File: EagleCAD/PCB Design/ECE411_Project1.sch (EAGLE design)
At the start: 38 parts, among them J1 0473460001_USBMICRO, U1 ATS160SM-1, U2 MIC29310-5.0WU, U3 NCP5501DT50RKG, U4 DCJACK_2.1MM_PTH

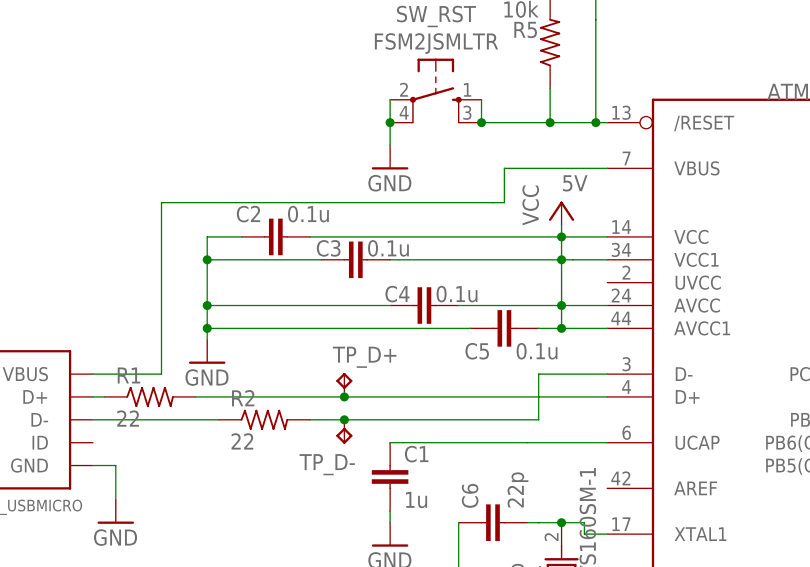
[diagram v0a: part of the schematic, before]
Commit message: In-progress updates: Connected UVCC to power and added a capacitor for it
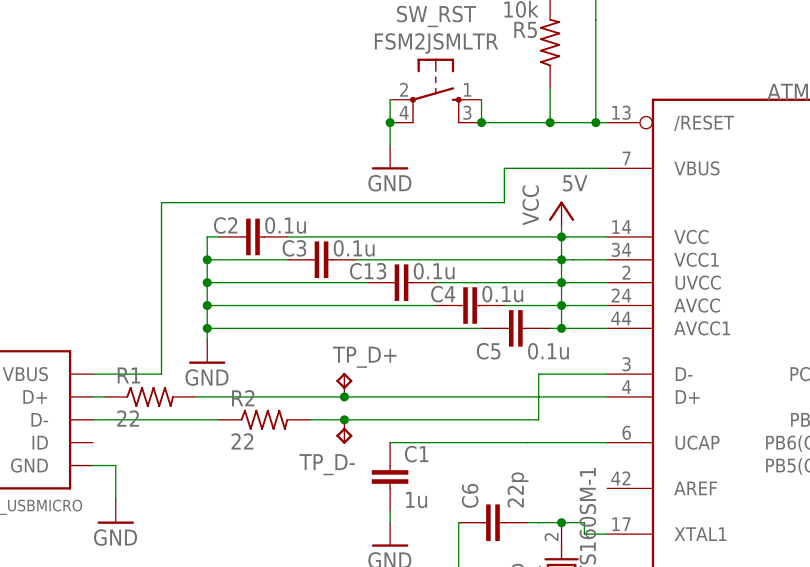
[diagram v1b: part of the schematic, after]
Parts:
- added C13: 0.1u, rcl:C-EUC1206
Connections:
- net GND: now also C13.1
- net VCC: now also C13.2, U$1.UVCC
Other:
- moved on the sheet: C2, C3, C4, C5
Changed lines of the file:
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@@
 <part name="C12" library="ElectrolyticCap" deviceset="UWT1V100MCL1GB" device="" value="10uF"/>
 <part name="GND16" library="supply1" library_urn="urn:adsk.eagle:library:371" deviceset="GND" device=""/>
+<part name="C13" library="rcl" library_urn="urn:adsk.eagle:library:334" deviceset="C-EU" device="C1206" package3d_urn="urn:adsk.eagle:package:23618/2" value="0.1u">
+<spice>
+<pinmapping spiceprefix="C">
+<pinmap gate="G$1" pin="1" pinorder="1"/>
+<pinmap gate="G$1" pin="2" pinorder="2"/>
+</pinmapping>
+</spice>
+<attribute name="COST" value=""/>
+<attribute name="PART_NO" value=""/>
+<attribute name="VENDER" value="Arrow"/>
+</part>
 </parts>
 <sheets>
@@
 <attribute name="VALUE" x="-68.58" y="54.61" size="1.778" layer="96"/>
 </instance>
-<instance part="C2" gate="G$1" x="-59.69" y="71.12" smashed="yes" rot="R90">
-<attribute name="NAME" x="-59.944" y="74.549" size="1.778" layer="95" rot="R180"/>
-<attribute name="VALUE" x="-52.324" y="74.549" size="1.778" layer="96" rot="R180"/>
-<attribute name="COST" x="-59.69" y="71.12" size="1.778" layer="96" rot="R90" display="off"/>
-<attribute name="PART_NO" x="-59.69" y="71.12" size="1.778" layer="96" rot="R90" display="off"/>
-<attribute name="VENDER" x="-59.69" y="71.12" size="1.778" layer="96" rot="R90" display="off"/>
+<instance part="C2" gate="G$1" x="-62.23" y="71.12" smashed="yes" rot="R90">
+<attribute name="NAME" x="-62.484" y="73.279" size="1.778" layer="95" rot="R180"/>
+<attribute name="VALUE" x="-54.864" y="73.279" size="1.778" layer="96" rot="R180"/>
+<attribute name="COST" x="-62.23" y="71.12" size="1.778" layer="96" rot="R90" display="off"/>
+<attribute name="PART_NO" x="-62.23" y="71.12" size="1.778" layer="96" rot="R90" display="off"/>
+<attribute name="VENDER" x="-62.23" y="71.12" size="1.778" layer="96" rot="R90" display="off"/>
 </instance>
 <instance part="R1" gate="G$1" x="-72.39" y="53.34" smashed="yes">
@@
 <attribute name="NAME" x="43.18" y="11.43" size="1.778" layer="95"/>
 </instance>
-<instance part="C3" gate="G$1" x="-50.8" y="68.58" smashed="yes" rot="R90">
-<attribute name="NAME" x="-51.054" y="70.739" size="1.778" layer="95" rot="R180"/>
-<attribute name="VALUE" x="-43.434" y="70.739" size="1.778" layer="96" rot="R180"/>
-<attribute name="COST" x="-50.8" y="68.58" size="1.778" layer="96" rot="R90" display="off"/>
-<attribute name="PART_NO" x="-50.8" y="68.58" size="1.778" layer="96" rot="R90" display="off"/>
-<attribute name="VENDER" x="-50.8" y="68.58" size="1.778" layer="96" rot="R90" display="off"/>
-</instance>
-<instance part="C4" gate="G$1" x="-43.18" y="63.5" smashed="yes" rot="R90">
-<attribute name="NAME" x="-43.434" y="65.659" size="1.778" layer="95" rot="R180"/>
-<attribute name="VALUE" x="-35.814" y="65.659" size="1.778" layer="96" rot="R180"/>
-<attribute name="COST" x="-43.18" y="63.5" size="1.778" layer="96" rot="R90" display="off"/>
-<attribute name="PART_NO" x="-43.18" y="63.5" size="1.778" layer="96" rot="R90" display="off"/>
-<attribute name="VENDER" x="-43.18" y="63.5" size="1.778" layer="96" rot="R90" display="off"/>
-</instance>
-<instance part="C5" gate="G$1" x="-34.29" y="60.96" smashed="yes" rot="R90">
-<attribute name="NAME" x="-34.544" y="59.309" size="1.778" layer="95" rot="R180"/>
-<attribute name="VALUE" x="-26.924" y="59.309" size="1.778" layer="96" rot="R180"/>
-<attribute name="COST" x="-34.29" y="60.96" size="1.778" layer="96" rot="R90" display="off"/>
-<attribute name="PART_NO" x="-34.29" y="60.96" size="1.778" layer="96" rot="R90" display="off"/>
-<attribute name="VENDER" x="-34.29" y="60.96" size="1.778" layer="96" rot="R90" display="off"/>
+<instance part="C3" gate="G$1" x="-54.61" y="68.58" smashed="yes" rot="R90">
+<attribute name="NAME" x="-54.864" y="70.739" size="1.778" layer="95" rot="R180"/>
+<attribute name="VALUE" x="-47.244" y="70.739" size="1.778" layer="96" rot="R180"/>
+<attribute name="COST" x="-54.61" y="68.58" size="1.778" layer="96" rot="R90" display="off"/>
+<attribute name="PART_NO" x="-54.61" y="68.58" size="1.778" layer="96" rot="R90" display="off"/>
+<attribute name="VENDER" x="-54.61" y="68.58" size="1.778" layer="96" rot="R90" display="off"/>
+</instance>
+<instance part="C4" gate="G$1" x="-38.1" y="63.5" smashed="yes" rot="R90">
+<attribute name="NAME" x="-38.354" y="65.659" size="1.778" layer="95" rot="R180"/>
+<attribute name="VALUE" x="-30.734" y="65.659" size="1.778" layer="96" rot="R180"/>
+<attribute name="COST" x="-38.1" y="63.5" size="1.778" layer="96" rot="R90" display="off"/>
+<attribute name="PART_NO" x="-38.1" y="63.5" size="1.778" layer="96" rot="R90" display="off"/>
+<attribute name="VENDER" x="-38.1" y="63.5" size="1.778" layer="96" rot="R90" display="off"/>
+</instance>
+<instance part="C5" gate="G$1" x="-33.02" y="60.96" smashed="yes" rot="R90">
+<attribute name="NAME" x="-33.274" y="59.309" size="1.778" layer="95" rot="R180"/>
+<attribute name="VALUE" x="-25.654" y="59.309" size="1.778" layer="96" rot="R180"/>
+<attribute name="COST" x="-33.02" y="60.96" size="1.778" layer="96" rot="R90" display="off"/>
+<attribute name="PART_NO" x="-33.02" y="60.96" size="1.778" layer="96" rot="R90" display="off"/>
+<attribute name="VENDER" x="-33.02" y="60.96" size="1.778" layer="96" rot="R90" display="off"/>
 </instance>
 <instance part="C12" gate="G$1" x="17.78" y="115.57"/>
 <instance part="GND16" gate="1" x="17.78" y="106.68" smashed="yes">
 <attribute name="VALUE" x="15.24" y="104.14" size="1.778" layer="96"/>
+</instance>
+<instance part="C13" gate="G$1" x="-45.72" y="66.04" smashed="yes" rot="R90">
+<attribute name="NAME" x="-45.974" y="68.199" size="1.778" layer="95" rot="R180"/>
+<attribute name="VALUE" x="-38.354" y="68.199" size="1.778" layer="96" rot="R180"/>
+<attribute name="COST" x="-45.72" y="66.04" size="1.778" layer="96" rot="R90" display="off"/>
+<attribute name="PART_NO" x="-45.72" y="66.04" size="1.778" layer="96" rot="R90" display="off"/>
+<attribute name="VENDER" x="-45.72" y="66.04" size="1.778" layer="96" rot="R90" display="off"/>
 </instance>
 </instances>
@@
 <segment>
 <pinref part="C2" gate="G$1" pin="1"/>
-<wire x1="-62.23" y1="71.12" x2="-66.04" y2="71.12" width="0.1524" layer="91"/>
+<wire x1="-64.77" y1="71.12" x2="-66.04" y2="71.12" width="0.1524" layer="91"/>
 <pinref part="GND13" gate="1" pin="GND"/>
 <wire x1="-66.04" y1="71.12" x2="-66.04" y2="68.58" width="0.1524" layer="91"/>
-<wire x1="-66.04" y1="68.58" x2="-66.04" y2="63.5" width="0.1524" layer="91"/>
+<wire x1="-66.04" y1="68.58" x2="-66.04" y2="66.04" width="0.1524" layer="91"/>
+<wire x1="-66.04" y1="66.04" x2="-66.04" y2="63.5" width="0.1524" layer="91"/>
 <wire x1="-66.04" y1="63.5" x2="-66.04" y2="60.96" width="0.1524" layer="91"/>
 <wire x1="-66.04" y1="60.96" x2="-66.04" y2="59.69" width="0.1524" layer="91"/>
-<wire x1="-36.83" y1="60.96" x2="-66.04" y2="60.96" width="0.1524" layer="91"/>
+<wire x1="-35.56" y1="60.96" x2="-66.04" y2="60.96" width="0.1524" layer="91"/>
 <junction x="-66.04" y="60.96"/>
-<wire x1="-45.72" y1="63.5" x2="-66.04" y2="63.5" width="0.1524" layer="91"/>
+<wire x1="-40.64" y1="63.5" x2="-66.04" y2="63.5" width="0.1524" layer="91"/>
 <junction x="-66.04" y="63.5"/>
-<wire x1="-53.34" y1="68.58" x2="-66.04" y2="68.58" width="0.1524" layer="91"/>
+<wire x1="-57.15" y1="68.58" x2="-66.04" y2="68.58" width="0.1524" layer="91"/>
 <junction x="-66.04" y="68.58"/>
 <pinref part="C3" gate="G$1" pin="1"/>
 <pinref part="C4" gate="G$1" pin="1"/>
 <pinref part="C5" gate="G$1" pin="1"/>
+<pinref part="C13" gate="G$1" pin="1"/>
+<wire x1="-48.26" y1="66.04" x2="-66.04" y2="66.04" width="0.1524" layer="91"/>
+<junction x="-66.04" y="66.04"/>
 </segment>
 <segment>
@@
 <wire x1="-26.67" y1="60.96" x2="-21.59" y2="60.96" width="0.1524" layer="91"/>
 <pinref part="C2" gate="G$1" pin="2"/>
-<wire x1="-54.61" y1="71.12" x2="-26.67" y2="71.12" width="0.1524" layer="91"/>
+<wire x1="-57.15" y1="71.12" x2="-26.67" y2="71.12" width="0.1524" layer="91"/>
 <junction x="-26.67" y="71.12"/>
 <pinref part="P+2" gate="VCC" pin="VCC"/>
 <wire x1="-26.67" y1="71.12" x2="-26.67" y2="72.39" width="0.1524" layer="91"/>
-<wire x1="-45.72" y1="68.58" x2="-26.67" y2="68.58" width="0.1524" layer="91"/>
-<wire x1="-38.1" y1="63.5" x2="-26.67" y2="63.5" width="0.1524" layer="91"/>
-<wire x1="-29.21" y1="60.96" x2="-26.67" y2="60.96" width="0.1524" layer="91"/>
+<wire x1="-49.53" y1="68.58" x2="-26.67" y2="68.58" width="0.1524" layer="91"/>
+<wire x1="-33.02" y1="63.5" x2="-26.67" y2="63.5" width="0.1524" layer="91"/>
+<wire x1="-27.94" y1="60.96" x2="-26.67" y2="60.96" width="0.1524" layer="91"/>
 <junction x="-26.67" y="60.96"/>
 <pinref part="C3" gate="G$1" pin="2"/>
 <pinref part="C4" gate="G$1" pin="2"/>
 <pinref part="C5" gate="G$1" pin="2"/>
-</segment>
-<segment>
+<pinref part="U$1" gate="G$1" pin="UVCC"/>
+<wire x1="-21.59" y1="66.04" x2="-26.67" y2="66.04" width="0.1524" layer="91"/>
+<junction x="-26.67" y="66.04"/>
+<pinref part="C13" gate="G$1" pin="2"/>
+<wire x1="-40.64" y1="66.04" x2="-26.67" y2="66.04" width="0.1524" layer="91"/>
+</segment>
+<segment>
